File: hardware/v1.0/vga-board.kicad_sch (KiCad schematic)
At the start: 15 parts, among them J10 Conn_01x06, J9 Conn_01x34, U6 74LVC245A, U7 TLV62585

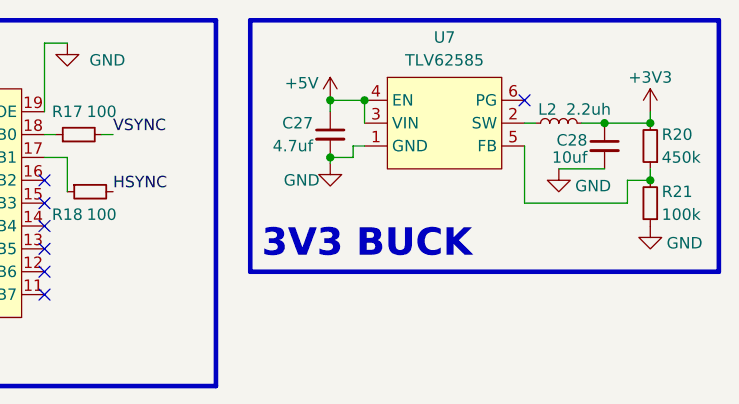
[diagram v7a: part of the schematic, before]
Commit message: redoing 3v3 regulators
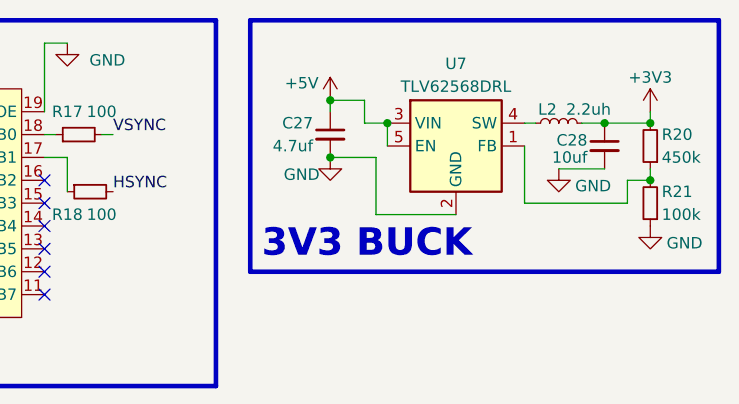
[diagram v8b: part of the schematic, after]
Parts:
- removed U7: TLV62585, Package_TO_SOT_SMD:SOT-563, symbol mylib:TLV62585
- added U7: TLV62568DRL, Package_TO_SOT_SMD:SOT-563, symbol Regulator_Switching:TLV62568DRL
- C27, C28: footprint Capacitor_SMD:C_0805_2012Metric -> Capacitor_SMD:C_0603_1608Metric
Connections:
- net +5V: now also U7.3 (VIN), U7.5 (EN)
- net GND: now also U7.2 (GND)
- net at R20.1, R21.2: now also U7.1 (FB)
- net at L2.1: now also U7.4 (SW)
- no-connect marks 15 -> 14
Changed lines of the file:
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@@
 	)
 	(junction
-		(at 203.2 30.48)
-		(diameter 0)
-		(color 0 0 0 0)
-	)
-	(junction
 		(at 133.35 50.8)
 		(diameter 0)
@@
 	)
 	(junction
+		(at 203.2 30.48)
+		(diameter 0)
+		(color 0 0 0 0)
+	)
+	(junction
 		(at 238.76 33.02)
 		(diameter 0)
@@
 	)
 	(junction
-		(at 207.01 24.13)
+		(at 238.76 26.67)
 		(diameter 0)
 		(color 0 0 0 0)
 	)
 	(junction
-		(at 238.76 26.67)
+		(at 209.55 26.67)
 		(diameter 0)
 		(color 0 0 0 0)
@@
 	)
 	(no_connect
-		(at 224.79 24.13)
-	)
-	(no_connect
 		(at 148.59 38.1)
 	)
@@
 		)
 	)
+	(wire
+		(pts
+			(xy 208.28 30.48) (xy 203.2 30.48)
+		)
+		(stroke
+			(width 0)
+			(type default)
+		)
+	)
 	(bus
 		(pts
@@
 		)
 	)
-	(wire
-		(pts
-			(xy 205.74 29.21) (xy 205.74 30.48)
-		)
-		(stroke
-			(width 0)
-			(type default)
-		)
-	)
 	(bus
 		(pts
@@
 	(wire
 		(pts
-			(xy 203.2 30.48) (xy 203.2 31.115)
-		)
-		(stroke
-			(width 0)
-			(type default)
-		)
-	)
-	(wire
-		(pts
 			(xy 146.685 25.4) (xy 148.59 25.4)
 		)
@@
 	(wire
 		(pts
+			(xy 217.17 36.83) (xy 208.28 36.83)
+		)
+		(stroke
+			(width 0)
+			(type default)
+		)
+	)
+	(wire
+		(pts
 			(xy 75.565 104.14) (xy 88.9 104.14)
 		)
@@
 		)
 	)
+	(wire
+		(pts
+			(xy 209.55 29.21) (xy 209.55 26.67)
+		)
+		(stroke
+			(width 0)
+			(type default)
+		)
+	)
 	(bus
 		(pts
@@
 	(wire
 		(pts
-			(xy 203.2 30.48) (xy 205.74 30.48)
-		)
-		(stroke
-			(width 0)
-			(type default)
-		)
-	)
-	(wire
-		(pts
 			(xy 22.86 43.18) (xy 36.83 43.18)
 		)
@@
 	(wire
 		(pts
-			(xy 207.01 29.21) (xy 205.74 29.21)
+			(xy 22.86 58.42) (xy 36.83 58.42)
 		)
 		(stroke
@@
 		)
 	)
-	(wire
+	(bus
 		(pts
-			(xy 22.86 58.42) (xy 36.83 58.42)
+			(xy 39.37 60.96) (xy 39.37 66.04)
 		)
 		(stroke
@@
 		)
 	)
-	(bus
+	(wire
 		(pts
-			(xy 39.37 60.96) (xy 39.37 66.04)
+			(xy 208.28 36.83) (xy 208.28 30.48)
 		)
 		(stroke
@@
 	(wire
 		(pts
+			(xy 209.55 26.67) (xy 207.01 26.67)
+		)
+		(stroke
+			(width 0)
+			(type default)
+		)
+	)
+	(wire
+		(pts
 			(xy 173.99 64.77) (xy 171.45 64.77)
 		)
@@
 	)
 	(symbol
+		(lib_id "Regulator_Switching:TLV62568DRL")
+		(at 217.17 29.21 0)
+		(unit 1)
+		(exclude_from_sim no)
+		(in_bom yes)
+		(on_board yes)
+		(dnp no)
+		(property "Reference" "U7"
+			(at 217.17 20.066 0)
+			(effects
+				(font
+					(size 1.27 1.27)
+				)
+			)
+		)
+		(property "Value" "TLV62568DRL"
+			(at 217.17 22.606 0)
+			(effects
+				(font
+					(size 1.27 1.27)
+				)
+			)
+		)
+		(property "Footprint" "Package_TO_SOT_SMD:SOT-563"
+			(at 218.44 35.56 0)
+			(effects
+				(font
+					(size 1.27 1.27)
+					(italic yes)
+				)
+				(justify left)
+				(hide yes)
+			)
+		)
+		(property "Datasheet" "http://www.ti.com/lit/ds/symlink/tlv62568.pdf"
+			(at 210.82 17.78 0)
+			(effects
+				(font
+					(size 1.27 1.27)
+				)
+				(hide yes)
+			)
+		)
+		(property "Description" "High Efficiency Synchronous Buck Converter, Adjustable Output 0.6V-5.5V, 1A, SOT-563-6"
+			(at 217.17 29.21 0)
+			(effects
+				(font
+					(size 1.27 1.27)
+				)
+				(hide yes)
+			)
+		)
+		(pin "3"
+		)
+		(pin "5"
+		)
+		(pin "1"
+		)
+		(pin "4"
+		)
+		(pin "6"
+		)
+		(pin "2"
+		)
+		(instances
+			(project "QMTECH_XC7A100T-Expantion-Board"
+				(path "/1a66a179-6cc4-4048-836e-3eb434e9da88/78456f10-420c-464d-bfaa-46b2e05e0014"
+					(reference "U7")
+					(unit 1)
+				)
+			)
+		)
+	)
+	(symbol
 		(lib_id "power:GND")
 		(at 133.35 50.8 0)
@@
 	(symbol
 		(lib_id "power:GND")
-		(at 203.2 31.115 0)
+		(at 203.2 30.48 0)
 		(unit 1)
 		(exclude_from_sim no)
@@
 		(dnp no)
 		(property "Reference" "#PWR63"
-			(at 203.2 37.465 0)
+			(at 203.2 36.83 0)
 			(effects
 				(font
@@
 		)
 		(property "Value" "GND"
-			(at 200.025 33.02 0)
+			(at 200.025 32.385 0)
 			(effects
 				(font
@@
 		)
 		(property "Footprint" ""
-			(at 203.2 31.115 0)
+			(at 203.2 30.48 0)
 			(effects
 				(font
@@
 		)
 		(property "Datasheet" ""
-			(at 203.2 31.115 0)
+			(at 203.2 30.48 0)
 			(effects
 				(font
@@
 		)
 		(property "Description" "Power symbol creates a global label with name \"GND\" , ground"
-			(at 203.2 31.115 0)
+			(at 203.2 30.48 0)
 			(effects
 				(font
@@
 			)
 		)
-		(property "Footprint" "Capacitor_SMD:C_0805_2012Metric"
+		(property "Footprint" "Capacitor_SMD:C_0603_1608Metric"
 			(at 233.68 29.21 0)
 			(effects
@@
 			)
 		)
-		(property "Footprint" "Capacitor_SMD:C_0805_2012Metric"
+		(property "Footprint" "Capacitor_SMD:C_0603_1608Metric"
 			(at 203.2 27.94 0)
 			(effects
@@
 					(unit 1)
 				)
-			)
-		)
-	)
-	(symbol
-		(lib_id "mylib:TLV62585")
-		(at 215.9 26.67 0)
-		(unit 1)
-		(exclude_from_sim no)
-		(in_bom yes)
-		(on_board yes)
-		(dnp no)
-		(fields_autoplaced yes)
-		(property "Reference" "U7"
-			(at 215.9 17.145 0)
-			(effects
-				(font
-					(size 1.27 1.27)
-				)
-			)
-		)
-		(property "Value" "TLV62585"
-			(at 215.9 19.685 0)
-			(effects
-				(font
-					(size 1.27 1.27)
-				)
-			)
-		)
-		(property "Footprint" "Package_TO_SOT_SMD:SOT-563"
-			(at 215.9 26.67 0)
-			(effects
-				(font
-					(size 1.27 1.27)
-				)
-				(hide yes)
-			)
-		)
-		(property "Datasheet" ""
-			(at 215.9 26.67 0)
-			(effects
-				(font
-					(size 1.27 1.27)
-				)
-				(hide yes)
-			)
-		)
-		(property "Description" ""
-			(at 215.9 26.67 0)
-			(effects
-				(font
-					(size 1.27 1.27)
-				)
-				(hide yes)
-			)
-		)
-		(pin "5"
-		)
-		(pin "1"
-		)
-		(pin "6"
-		)
-		(pin "3"
-		)
-		(pin "2"
-		)
-		(pin "4"
-		)
-		(instances
-			(project "QMTECH_XC7A100T-Expantion-Board"
-				(path "/1a66a179-6cc4-4048-836e-3eb434e9da88/78456f10-420c-464d-bfaa-46b2e05e0014"
-					(reference "U7")
-					(unit 1)
-				)
